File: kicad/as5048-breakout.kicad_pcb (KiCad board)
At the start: 2 copper layers, 30 x 30 mm, 12 parts, among them J1 Conn_01x05, SW1 ADDR SELECT, U1 AS5048B

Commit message: finalizing this
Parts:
- moved SW1 0.14 mm to (50.4, 37.0)

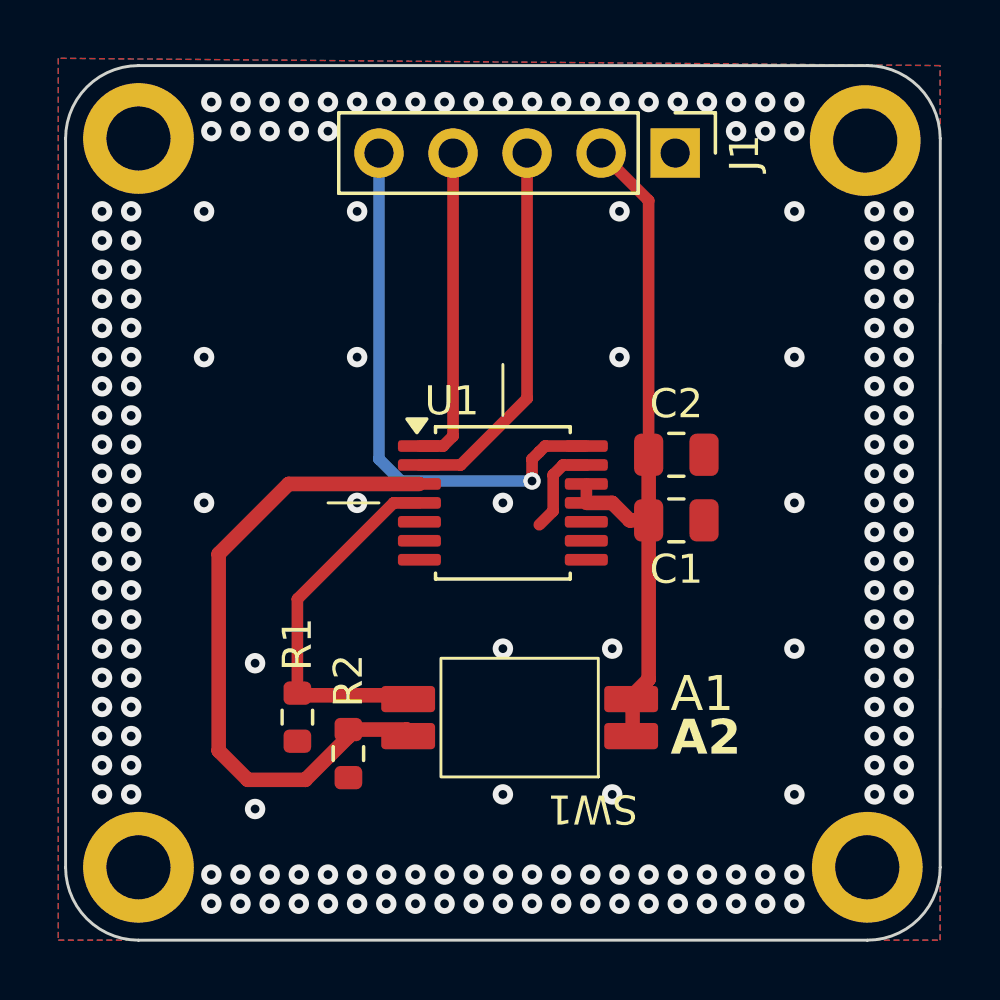
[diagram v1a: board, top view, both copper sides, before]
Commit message: feat: change pinheader to JST SH 1x4
with same pinouts as the Adafruit Qwiic or Stemma
connectors so that they could be used with their boards
(different pitch connectors used)
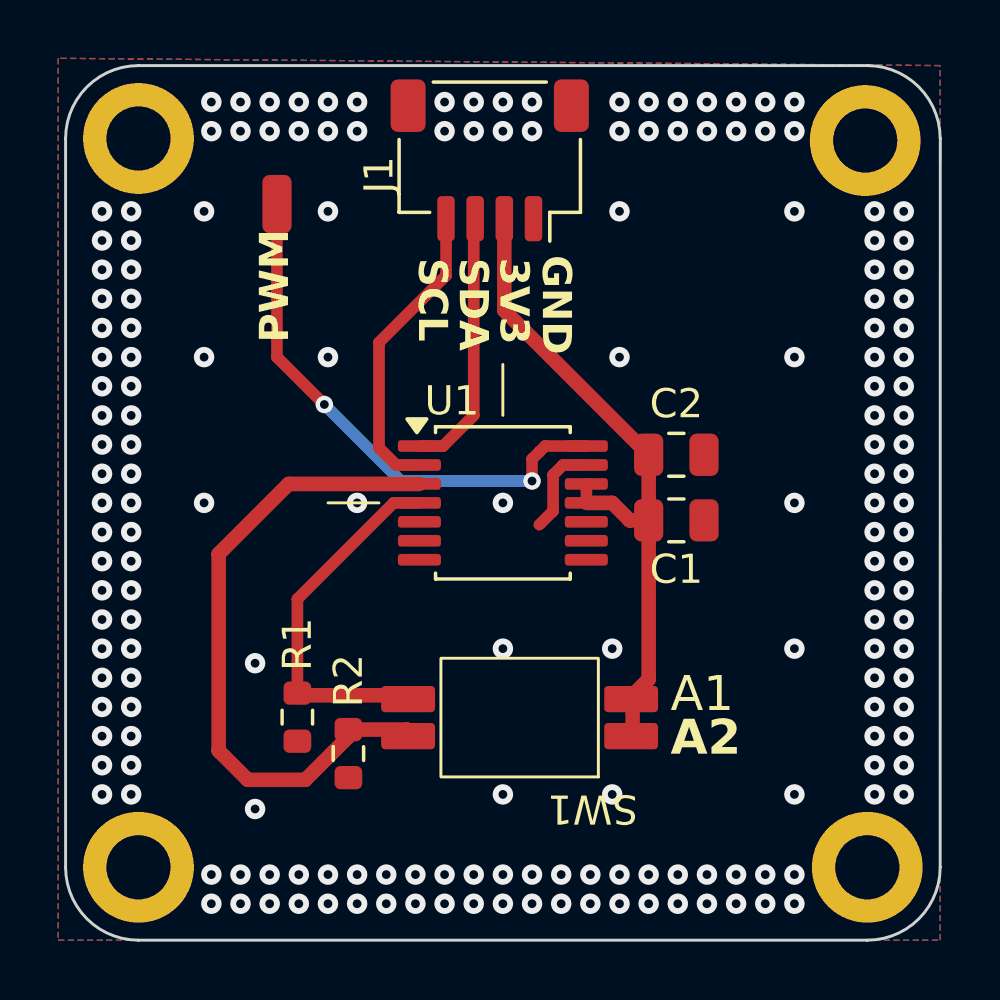
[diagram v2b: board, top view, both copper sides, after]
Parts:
- added J2: PWM, Connector_Wire:SolderWirePad_1x01_SMD_1x2mm, F.Cu at (38.2, 18.8)
- J1: value Conn_01x05 -> IIC; footprint Connector_PinHeader_2.54mm:PinHeader_1x05_P2.54mm_Vertical -> Connector_JST:JST_SH_SM04B-SRSS-TB_1x04-1MP_P1.00mm_Horizontal
- moved J1 6.36 mm to (45.5, 17.2), turned to 180 degrees
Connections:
- J1 pad 3: I2C_SCL -> I2C_SDA
- J1 pad 4: I2C_SDA -> I2C_SCL
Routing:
- net I2C_SCL: track 13.1 -> 10.4 mm
- net I2C_SDA: track 11.0 -> 9.05 mm
- net +3V3: track 23.9 -> 23.0 mm
- net PWM_OUT: track 18.9 -> 18.6 mm, vias 1 -> 2
- net GND: vias 175 -> 180
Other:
- board text added: "3V3"
- board text added: "GND"
- board text added: "PWM"
- board text added: "SCL"
- board text added: "SDA"
